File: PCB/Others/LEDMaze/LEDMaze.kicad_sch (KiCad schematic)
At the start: 74 parts

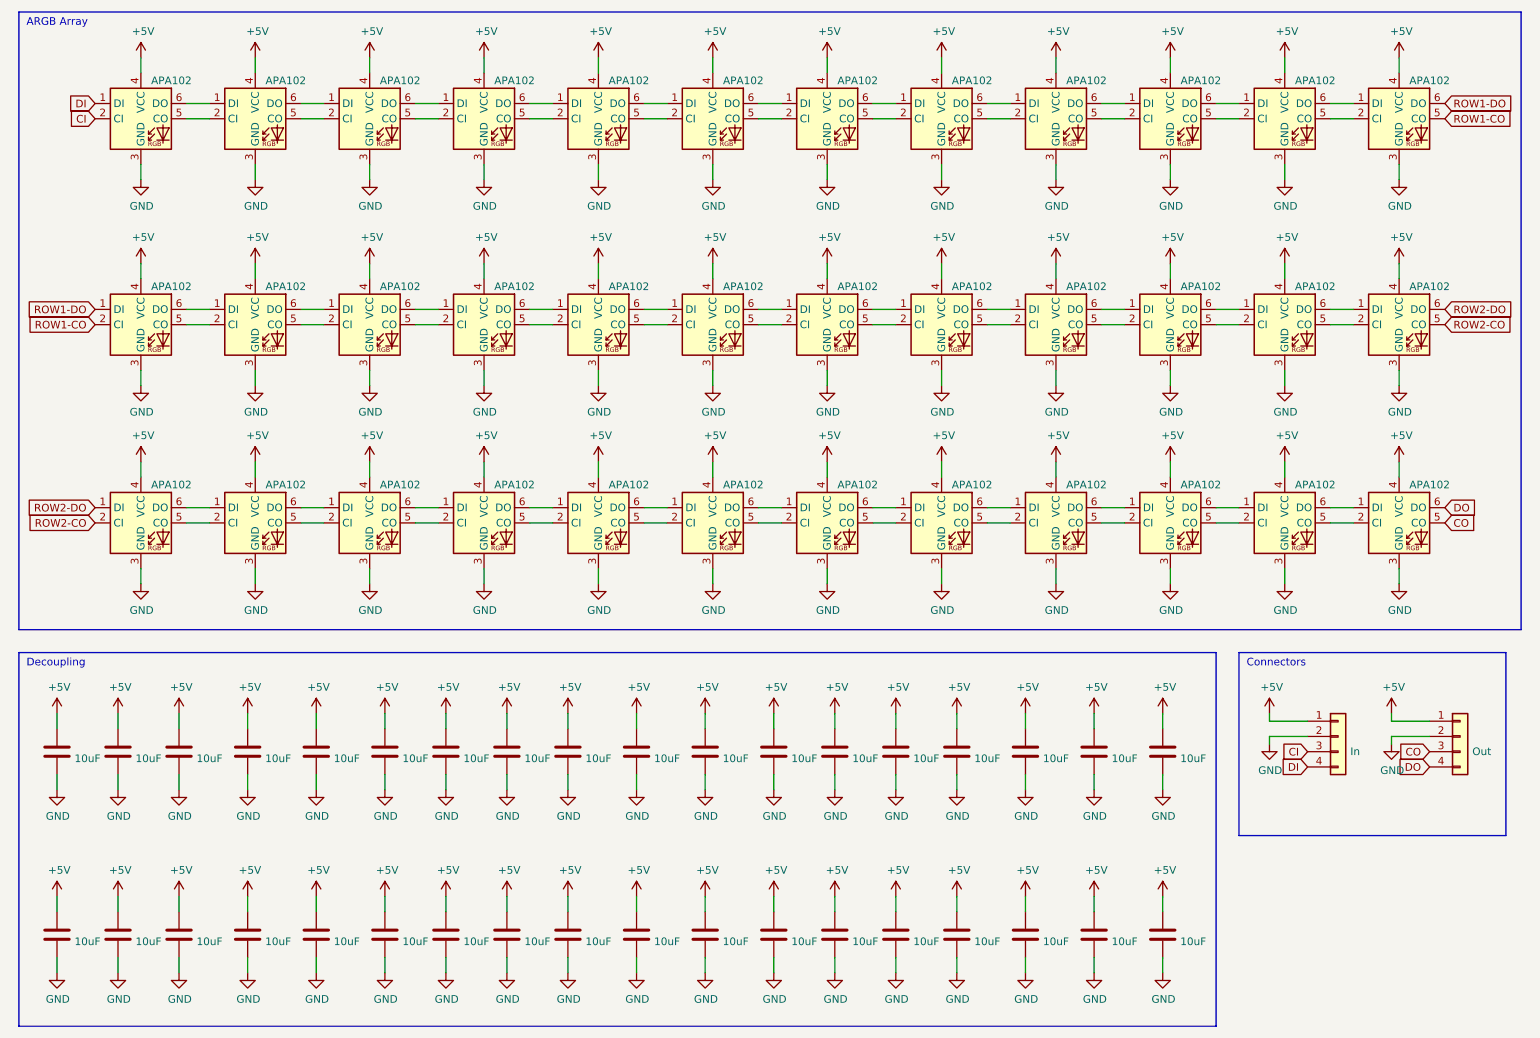
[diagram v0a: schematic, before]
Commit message: Upgrade KiCad files from 6.0 to 7.0.
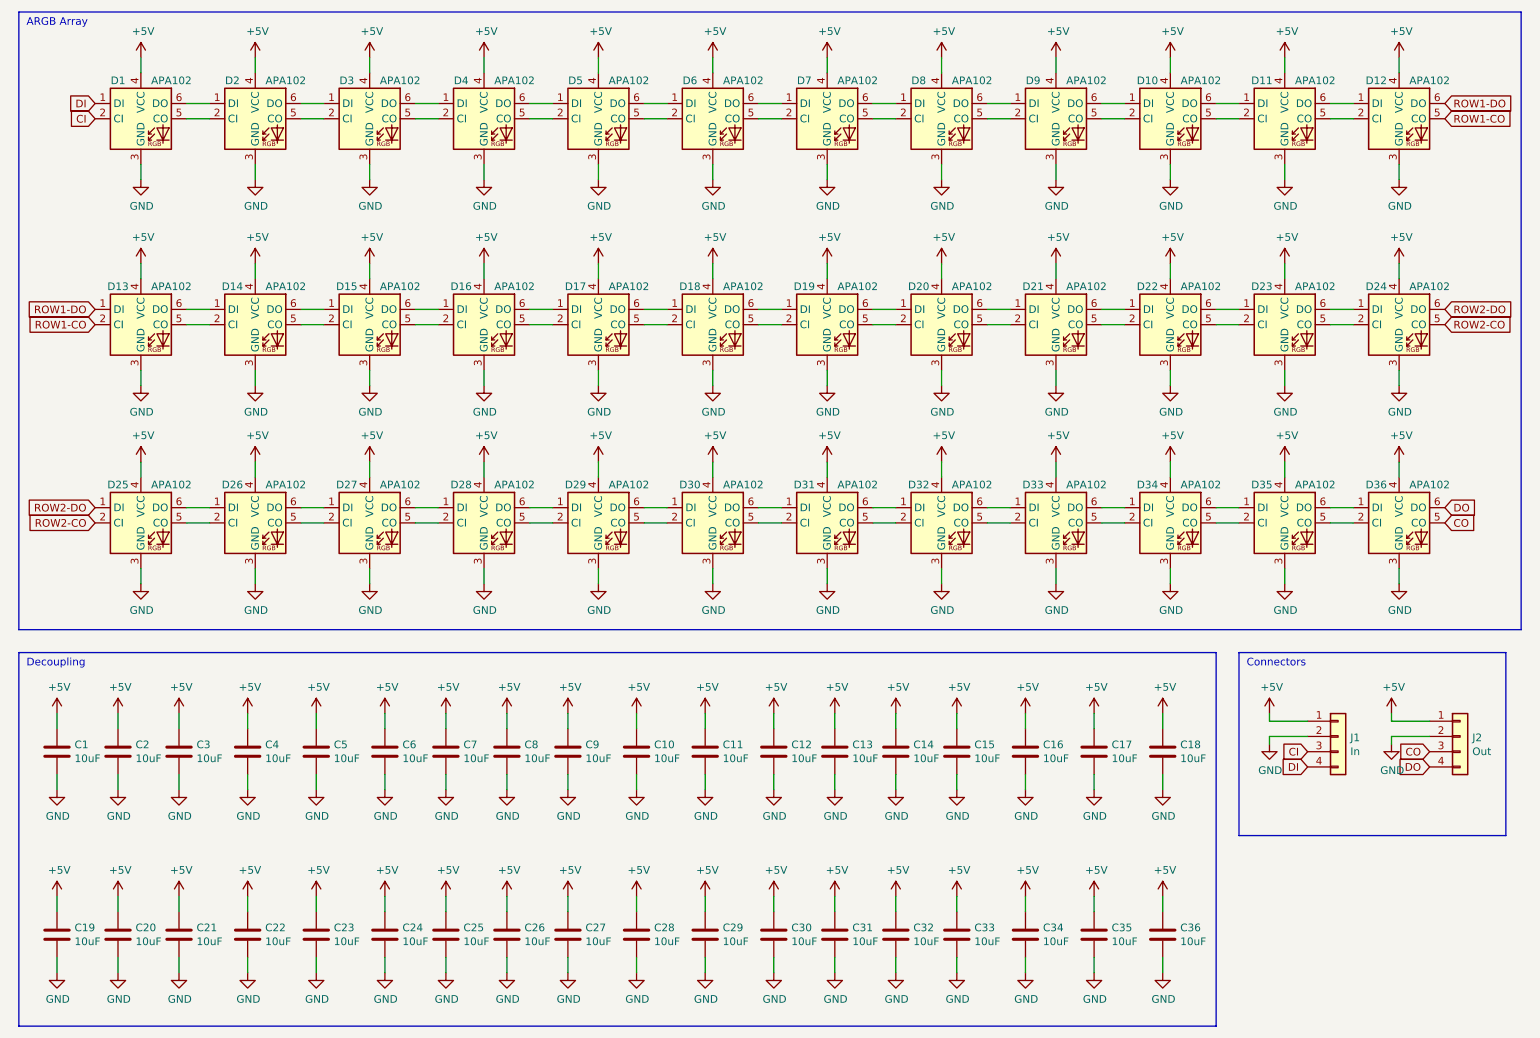
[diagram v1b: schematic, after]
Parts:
- gave numbers to parts that had none: 74
